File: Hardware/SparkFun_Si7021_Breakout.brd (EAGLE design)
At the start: 15.2 x 15.2 mm, 14 parts, among them U1 SI7021

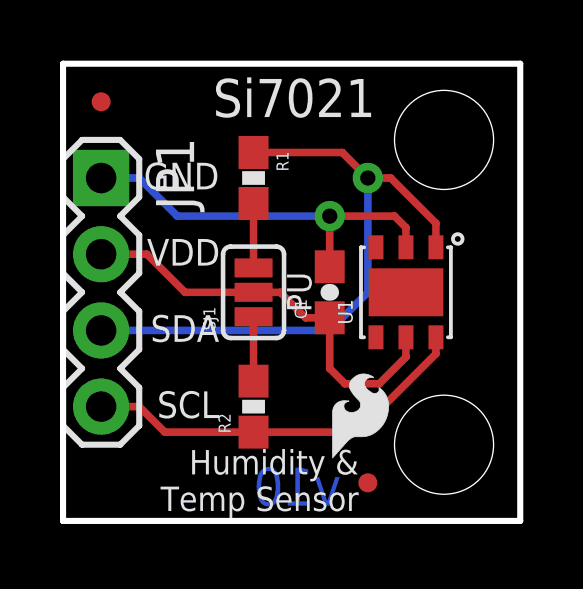
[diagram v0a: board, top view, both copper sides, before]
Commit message: Changes from Hardware Review with Toni
Lots of minor changes brought up during Toni’s Hardware review. See
repo issues for more details.
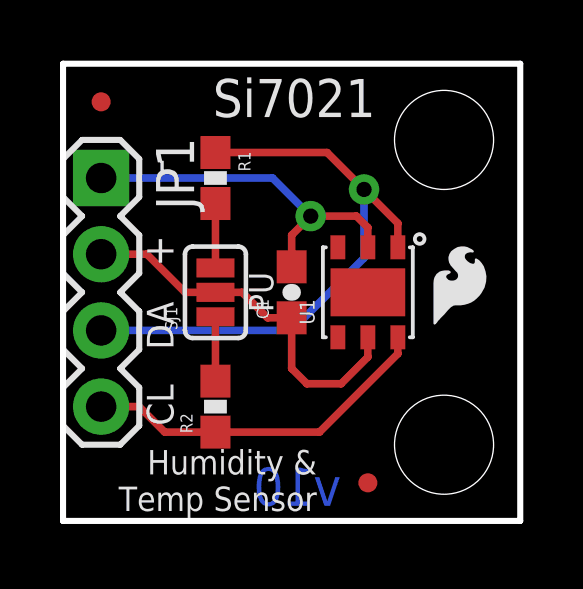
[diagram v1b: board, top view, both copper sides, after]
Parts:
- removed JP2: LOGO-SFENW2, SparkFun-Aesthetics:SFE-NEW-WEB
- removed LOGO1: LOGO-SFESK, SparkFun:SFE-LOGO-FLAME
- added LOGO3: SFE_LOGO_FLAME.1_INCH, SparkFun-Aesthetics:SFE_LOGO_FLAME_.1
- added LOGO4: SFE_LOGO_NAME.1_INCH, SparkFun-Aesthetics:SFE_LOGO_NAME_.1
- moved C1 1.27 mm to (7.62, 7.62)
- moved R1 1.27 mm to (5.08, 11.4)
- moved R2 1.27 mm to (5.08, 3.81)
- moved SJ1 1.27 mm to (5.08, 7.62)
- moved U1 1.27 mm to (10.2, 7.62)
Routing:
- net SCL: track 13.1 -> 11.9 mm
- net 3.3V: track 14.0 -> 12.7 mm
- net SDA: track 21.1 -> 19.9 mm
- net GND: track 13.2 -> 12.2 mm
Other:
- board text added: "+"
- board text added: "-"
- board text added: "CL"
- board text added: "DA"
- board text removed: "VDD"

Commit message: Changes from Hardware Review with Marshall
very minor changes - moved via, bumped trace with up near header, minor
spelling error on sch.
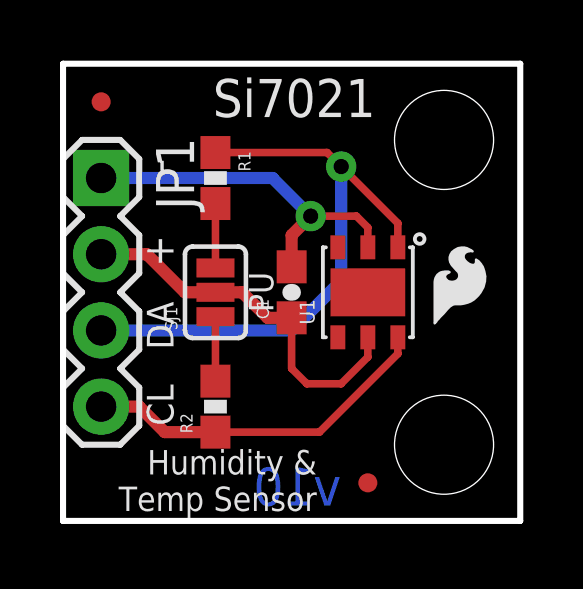
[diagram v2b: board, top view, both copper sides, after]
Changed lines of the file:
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@@
 <layer number="47" name="Measures" color="7" fill="1" visible="no" active="yes"/>
 <layer number="48" name="Document" color="7" fill="1" visible="no" active="yes"/>
-<layer number="49" name="Reference" color="7" fill="1" visible="yes" active="yes"/>
+<layer number="49" name="Reference" color="7" fill="1" visible="no" active="yes"/>
 <layer number="50" name="dxf" color="7" fill="1" visible="no" active="yes"/>
 <layer number="51" name="tDocu" color="6" fill="1" visible="yes" active="yes"/>
@@
 <element name="FRAME2" library="SparkFun-Aesthetics" package="CREATIVE_COMMONS" value="FRAME-LETTER" x="-12.7" y="-8.89"/>
 <element name="JP1" library="SparkFun-Connectors" package="1X04" value="" x="1.27" y="11.43" rot="R270"/>
-<element name="U1" library="SparkFun-Sensors" package="SI7021" value="SI7021" x="10.16" y="7.62" rot="R90"/>
+<element name="U1" library="SparkFun-Sensors" package="SI7021" value="SI7021" x="10.16" y="7.62" rot="R90">
+<attribute name="PROD_ID" value="IC-13093" x="10.16" y="7.62" size="1.778" layer="27" rot="R90" display="off"/>
+</element>
 <element name="LOGO3" library="SparkFun-Aesthetics" package="SFE_LOGO_FLAME_.1" value="SFE_LOGO_FLAME.1_INCH" x="12.065" y="6.223"/>
 <element name="LOGO4" library="SparkFun-Aesthetics" package="SFE_LOGO_NAME_.1" value="SFE_LOGO_NAME.1_INCH" x="8.89" y="13.97" rot="MR270"/>
@@
 <signal name="SCL">
 <contactref element="R2" pad="1"/>
-<wire x1="5.08" y1="2.96" x2="3.39" y2="2.96" width="0.254" layer="1"/>
-<wire x1="3.39" y1="2.96" x2="2.54" y2="3.81" width="0.254" layer="1"/>
+<wire x1="5.08" y1="2.96" x2="3.39" y2="2.96" width="0.4064" layer="1"/>
+<wire x1="3.39" y1="2.96" x2="2.54" y2="3.81" width="0.4064" layer="1"/>
 <wire x1="5.08" y1="2.96" x2="8.548" y2="2.96" width="0.254" layer="1"/>
 <wire x1="11.16" y1="5.572" x2="8.548" y2="2.96" width="0.254" layer="1"/>
@@
 <wire x1="11.16" y1="5.572" x2="11.16" y2="6.12" width="0.254" layer="1"/>
 <contactref element="JP1" pad="4"/>
-<wire x1="1.27" y1="3.81" x2="2.54" y2="3.81" width="0.254" layer="1"/>
+<wire x1="1.27" y1="3.81" x2="2.54" y2="3.81" width="0.4064" layer="1"/>
 </signal>
 <signal name="SDA">
 <contactref element="R1" pad="1"/>
+<contactref element="U1" pad="DATA"/>
+<contactref element="JP1" pad="3"/>
+<wire x1="1.27" y1="6.35" x2="7.62" y2="6.35" width="0.4064" layer="16"/>
+<via x="9.271" y="11.811" extent="1-16" drill="0.508"/>
+<wire x1="9.271" y1="8.001" x2="7.62" y2="6.35" width="0.4064" layer="16"/>
 <wire x1="5.08" y1="12.28" x2="8.802" y2="12.28" width="0.254" layer="1"/>
-<wire x1="7.62" y1="6.35" x2="10.033" y2="8.763" width="0.254" layer="16"/>
-<contactref element="U1" pad="DATA"/>
-<wire x1="11.16" y1="9.922" x2="11.16" y2="9.12" width="0.254" layer="1"/>
-<contactref element="JP1" pad="3"/>
-<wire x1="1.27" y1="6.35" x2="7.62" y2="6.35" width="0.254" layer="16"/>
-<wire x1="11.16" y1="9.922" x2="10.033" y2="11.049" width="0.254" layer="1"/>
-<via x="10.033" y="11.049" extent="1-16" drill="0.508"/>
-<wire x1="10.033" y1="11.049" x2="10.033" y2="8.763" width="0.254" layer="16"/>
-<wire x1="8.802" y1="12.28" x2="10.033" y2="11.049" width="0.254" layer="1"/>
+<wire x1="8.802" y1="12.28" x2="9.271" y2="11.811" width="0.254" layer="1"/>
+<wire x1="9.271" y1="11.811" x2="11.16" y2="9.922" width="0.254" layer="1"/>
+<wire x1="11.16" y1="9.12" x2="11.16" y2="9.922" width="0.254" layer="1"/>
+<wire x1="9.271" y1="8.001" x2="9.271" y2="11.811" width="0.4064" layer="16"/>
 </signal>
 <signal name="3.3V">
 <contactref element="C1" pad="1"/>
 <contactref element="SJ1" pad="2"/>
-<wire x1="5.08" y1="7.62" x2="4.064" y2="7.62" width="0.254" layer="1"/>
+<wire x1="5.08" y1="7.62" x2="4.064" y2="7.62" width="0.4064" layer="1"/>
 <wire x1="10.16" y1="5.461" x2="9.271" y2="4.572" width="0.254" layer="1"/>
 <wire x1="9.271" y1="4.572" x2="8.128" y2="4.572" width="0.254" layer="1"/>
 <wire x1="8.128" y1="4.572" x2="7.62" y2="5.08" width="0.254" layer="1"/>
 <wire x1="7.62" y1="5.08" x2="7.62" y2="6.77" width="0.254" layer="1"/>
-<wire x1="5.08" y1="7.62" x2="5.969" y2="7.62" width="0.254" layer="1"/>
-<wire x1="5.969" y1="7.62" x2="6.819" y2="6.77" width="0.254" layer="1"/>
-<wire x1="7.62" y1="6.77" x2="6.819" y2="6.77" width="0.254" layer="1"/>
+<wire x1="5.08" y1="7.62" x2="5.969" y2="7.62" width="0.4064" layer="1"/>
+<wire x1="5.969" y1="7.62" x2="6.819" y2="6.77" width="0.4064" layer="1"/>
+<wire x1="7.62" y1="6.77" x2="6.819" y2="6.77" width="0.4064" layer="1"/>
 <contactref element="U1" pad="VDD"/>
 <wire x1="10.16" y1="5.461" x2="10.16" y2="6.12" width="0.254" layer="1"/>
 <contactref element="JP1" pad="2"/>
-<wire x1="4.064" y1="7.62" x2="2.794" y2="8.89" width="0.254" layer="1"/>
-<wire x1="2.794" y1="8.89" x2="1.27" y2="8.89" width="0.254" layer="1"/>
+<wire x1="4.064" y1="7.62" x2="2.794" y2="8.89" width="0.4064" layer="1"/>
+<wire x1="2.794" y1="8.89" x2="1.27" y2="8.89" width="0.4064" layer="1"/>
 </signal>
 <signal name="N$1">
@@
 <contactref element="C1" pad="2"/>
 <contactref element="U1" pad="GND"/>
-<wire x1="1.27" y1="11.43" x2="6.985" y2="11.43" width="0.254" layer="16"/>
+<wire x1="1.27" y1="11.43" x2="6.985" y2="11.43" width="0.4064" layer="16"/>
 <via x="8.255" y="10.16" extent="1-16" drill="0.508"/>
 <wire x1="10.16" y1="9.12" x2="10.16" y2="9.779" width="0.254" layer="1"/>
 <wire x1="10.16" y1="9.779" x2="9.779" y2="10.16" width="0.254" layer="1"/>
 <wire x1="9.779" y1="10.16" x2="8.255" y2="10.16" width="0.254" layer="1"/>
-<wire x1="7.62" y1="8.47" x2="7.62" y2="9.525" width="0.254" layer="1"/>
-<wire x1="7.62" y1="9.525" x2="8.255" y2="10.16" width="0.254" layer="1"/>
-<wire x1="6.985" y1="11.43" x2="8.255" y2="10.16" width="0.254" layer="16"/>
+<wire x1="7.62" y1="8.47" x2="7.62" y2="9.525" width="0.4064" layer="1"/>
+<wire x1="7.62" y1="9.525" x2="8.255" y2="10.16" width="0.4064" layer="1"/>
+<wire x1="6.985" y1="11.43" x2="8.255" y2="10.16" width="0.4064" layer="16"/>
 </signal>
 </signals>

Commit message: Pushing minor changes from first QC check
Caps and resistors needed prod ID, version should be v01, not v10,
altered center pad on Si7021 IC to have 50% paste instead of 100%.
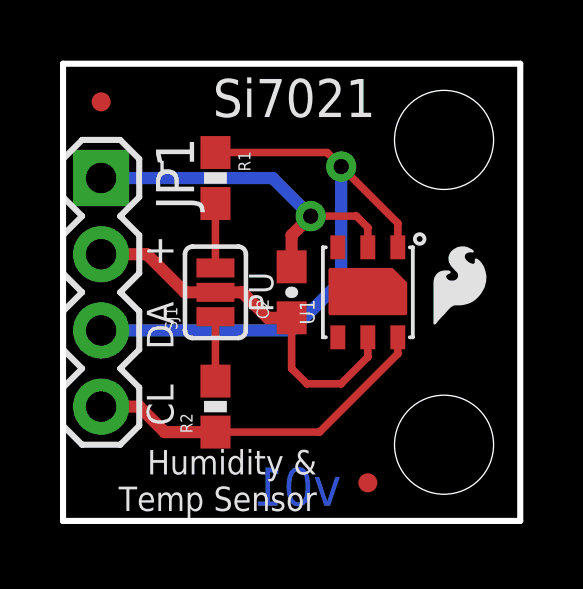
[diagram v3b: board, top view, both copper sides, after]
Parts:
- removed C1: 0.1uF, SparkFun:0603-CAP
- added C2: 0.1uF, SparkFun-Capacitors:0603-CAP
- R1, R2: value 4.7k -> 4.7K; device SparkFun:0603-RES -> SparkFun-Resistors:0603-RES
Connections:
- net 3.3V: now also C2.1; no longer C1.1
- net GND: now also C2.2; no longer C1.2
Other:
- board text added: "v01"
- board text removed: "v10"
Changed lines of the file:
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@@
 <layer number="47" name="Measures" color="7" fill="1" visible="no" active="yes"/>
 <layer number="48" name="Document" color="7" fill="1" visible="no" active="yes"/>
-<layer number="49" name="Reference" color="7" fill="1" visible="no" active="yes"/>
+<layer number="49" name="Reference" color="7" fill="1" visible="yes" active="yes"/>
 <layer number="50" name="dxf" color="7" fill="1" visible="no" active="yes"/>
 <layer number="51" name="tDocu" color="6" fill="1" visible="yes" active="yes"/>
@@
 <text x="2.667" y="12.065" size="1.016" layer="21" font="vector" ratio="15" rot="R270">-</text>
 <text x="17.78" y="-8.89" size="1.778" layer="51" font="vector">J. Bartlett</text>
-<text x="9.271" y="0.508" size="1.27" layer="16" ratio="20" rot="MR0">v10</text>
+<text x="9.271" y="0.508" size="1.27" layer="16" ratio="20" rot="MR0">v01</text>
 <text x="7.0104" y="6.9596" size="0.8128" layer="21" font="vector" ratio="15" rot="SR90">PU</text>
 <text x="8.4582" y="2.3622" size="0.8128" layer="21" font="vector" ratio="15" rot="R180">Humidity &amp;
@@
 </autorouter>
 <elements>
-<element name="C1" library="SparkFun" package="0603-CAP" value="0.1uF" x="7.62" y="7.62" rot="R90"/>
-<element name="R1" library="SparkFun" package="0603-RES" value="4.7k" x="5.08" y="11.43" rot="R270"/>
-<element name="R2" library="SparkFun" package="0603-RES" value="4.7k" x="5.08" y="3.81" rot="R90"/>
 <element name="SJ1" library="mike-temp" package="SJ_3_PASTE1&amp;2&amp;3" value="" x="5.08" y="7.62" rot="R90"/>
 <element name="STANDOFF2" library="SparkFun-Electromechanical" package="STAND-OFF" value="STAND-OFF" x="12.7" y="2.54" rot="R90"/>
@@
 <element name="LOGO3" library="SparkFun-Aesthetics" package="SFE_LOGO_FLAME_.1" value="SFE_LOGO_FLAME.1_INCH" x="12.065" y="6.223"/>
 <element name="LOGO4" library="SparkFun-Aesthetics" package="SFE_LOGO_NAME_.1" value="SFE_LOGO_NAME.1_INCH" x="8.89" y="13.97" rot="MR270"/>
+<element name="C2" library="SparkFun-Capacitors" package="0603-CAP" value="0.1uF" x="7.62" y="7.62" rot="R90">
+<attribute name="PROD_ID" value="CAP-00810" x="7.62" y="7.62" size="1.778" layer="27" font="vector" ratio="15" rot="R90" display="off"/>
+</element>
+<element name="R1" library="SparkFun-Resistors" package="0603-RES" value="4.7K" x="5.08" y="11.43" rot="R270">
+<attribute name="PROD_ID" value="RES-07857" x="5.08" y="11.43" size="1.778" layer="27" font="vector" ratio="15" rot="R270" display="off"/>
+</element>
+<element name="R2" library="SparkFun-Resistors" package="0603-RES" value="4.7K" x="5.08" y="3.81" rot="R90">
+<attribute name="PROD_ID" value="RES-07857" x="5.08" y="3.81" size="1.778" layer="27" font="vector" ratio="15" rot="R90" display="off"/>
+</element>
 </elements>
 <signals>
 <signal name="SCL">
-<contactref element="R2" pad="1"/>
-<wire x1="5.08" y1="2.96" x2="3.39" y2="2.96" width="0.4064" layer="1"/>
 <wire x1="3.39" y1="2.96" x2="2.54" y2="3.81" width="0.4064" layer="1"/>
-<wire x1="5.08" y1="2.96" x2="8.548" y2="2.96" width="0.254" layer="1"/>
 <wire x1="11.16" y1="5.572" x2="8.548" y2="2.96" width="0.254" layer="1"/>
 <contactref element="U1" pad="SCK"/>
@@
 <contactref element="JP1" pad="4"/>
 <wire x1="1.27" y1="3.81" x2="2.54" y2="3.81" width="0.4064" layer="1"/>
+<contactref element="R2" pad="1"/>
+<wire x1="8.548" y1="2.96" x2="5.08" y2="2.96" width="0.254" layer="1"/>
+<wire x1="5.08" y1="2.96" x2="3.39" y2="2.96" width="0.4064" layer="1"/>
 </signal>
 <signal name="SDA">
-<contactref element="R1" pad="1"/>
 <contactref element="U1" pad="DATA"/>
 <contactref element="JP1" pad="3"/>
@@
 <via x="9.271" y="11.811" extent="1-16" drill="0.508"/>
 <wire x1="9.271" y1="8.001" x2="7.62" y2="6.35" width="0.4064" layer="16"/>
-<wire x1="5.08" y1="12.28" x2="8.802" y2="12.28" width="0.254" layer="1"/>
 <wire x1="8.802" y1="12.28" x2="9.271" y2="11.811" width="0.254" layer="1"/>
 <wire x1="9.271" y1="11.811" x2="11.16" y2="9.922" width="0.254" layer="1"/>
 <wire x1="11.16" y1="9.12" x2="11.16" y2="9.922" width="0.254" layer="1"/>
 <wire x1="9.271" y1="8.001" x2="9.271" y2="11.811" width="0.4064" layer="16"/>
+<contactref element="R1" pad="1"/>
+<wire x1="5.08" y1="12.28" x2="8.802" y2="12.28" width="0.254" layer="1"/>
 </signal>
 <signal name="3.3V">
-<contactref element="C1" pad="1"/>
 <contactref element="SJ1" pad="2"/>
 <wire x1="5.08" y1="7.62" x2="4.064" y2="7.62" width="0.4064" layer="1"/>
@@
 <wire x1="9.271" y1="4.572" x2="8.128" y2="4.572" width="0.254" layer="1"/>
 <wire x1="8.128" y1="4.572" x2="7.62" y2="5.08" width="0.254" layer="1"/>
-<wire x1="7.62" y1="5.08" x2="7.62" y2="6.77" width="0.254" layer="1"/>
 <wire x1="5.08" y1="7.62" x2="5.969" y2="7.62" width="0.4064" layer="1"/>
 <wire x1="5.969" y1="7.62" x2="6.819" y2="6.77" width="0.4064" layer="1"/>
-<wire x1="7.62" y1="6.77" x2="6.819" y2="6.77" width="0.4064" layer="1"/>
 <contactref element="U1" pad="VDD"/>
 <wire x1="10.16" y1="5.461" x2="10.16" y2="6.12" width="0.254" layer="1"/>
@@
 <wire x1="4.064" y1="7.62" x2="2.794" y2="8.89" width="0.4064" layer="1"/>
 <wire x1="2.794" y1="8.89" x2="1.27" y2="8.89" width="0.4064" layer="1"/>
+<contactref element="C2" pad="1"/>
+<wire x1="7.62" y1="5.08" x2="7.62" y2="6.77" width="0.254" layer="1"/>
+<wire x1="6.819" y1="6.77" x2="7.62" y2="6.77" width="0.4064" layer="1"/>
 </signal>
 <signal name="N$1">
+<contactref element="SJ1" pad="3"/>
 <contactref element="R1" pad="2"/>
-<contactref element="SJ1" pad="3"/>
 <wire x1="5.08" y1="8.4328" x2="5.08" y2="10.58" width="0.254" layer="1"/>
 </signal>
 <signal name="N$2">
+<contactref element="SJ1" pad="1"/>
 <contactref element="R2" pad="2"/>
-<contactref element="SJ1" pad="1"/>
-<wire x1="5.08" y1="4.66" x2="5.08" y2="6.8072" width="0.254" layer="1"/>
+<wire x1="5.08" y1="6.8072" x2="5.08" y2="4.66" width="0.254" layer="1"/>
 </signal>
 <signal name="GND">
 <contactref element="JP1" pad="1"/>
-<contactref element="C1" pad="2"/>
 <contactref element="U1" pad="GND"/>
 <wire x1="1.27" y1="11.43" x2="6.985" y2="11.43" width="0.4064" layer="16"/>
@@
 <wire x1="10.16" y1="9.779" x2="9.779" y2="10.16" width="0.254" layer="1"/>
 <wire x1="9.779" y1="10.16" x2="8.255" y2="10.16" width="0.254" layer="1"/>
-<wire x1="7.62" y1="8.47" x2="7.62" y2="9.525" width="0.4064" layer="1"/>
 <wire x1="7.62" y1="9.525" x2="8.255" y2="10.16" width="0.4064" layer="1"/>
 <wire x1="6.985" y1="11.43" x2="8.255" y2="10.16" width="0.4064" layer="16"/>
+<contactref element="C2" pad="2"/>
+<wire x1="7.62" y1="9.525" x2="7.62" y2="8.47" width="0.4064" layer="1"/>
 </signal>
 </signals>
